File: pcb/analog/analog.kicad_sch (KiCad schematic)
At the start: 72 parts, among them J1 USB_C_Receptacle_USB2.0, SW1 SW_Push, SW2 SW_Push, U1 SRV05-4, U10 RP2040, U11 W25Q128JVS, U2 XC6206P332MR, U3 DRV5056A3xDBZxQ1, U4 DRV5056A3xDBZxQ1, U5 DRV5056A3xDBZxQ1, U6 74AHCT1G125, U7 74AHCT1G125, U8 74AHCT1G125, U9 74AHCT1G125, Y1 12MHz

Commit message: refactor: drive switch LEDs from a single output pin
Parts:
- removed R7, R8: 1k, Resistor_SMD:R_0402_1005Metric, symbol Device:R_Small
- removed U7, U8: 74AHCT1G125, Package_TO_SOT_SMD:SOT-353_SC-70-5, symbol 74xGxx:74AHCT1G125
- renumbered R12 to R10, R13 to R11, R14 to R12, R15 to R13, R16 to R14, R9 to R7, R10 to R8, R11 to R9, U9 to U7, U10 to U8, U11 to U9
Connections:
- net RGB_HS0: no longer U6.2
- net at LED1.2 (DOUT): now also LED2.3 (DIN)
- net at LED3.3 (DIN): now also LED2.2 (DOUT)
- net RGB_HS1: no longer names the net of U8.13 (GPIO10)
- net RGB_HS2: no longer names the net of U8.12 (GPIO9)
- new net RGB_HS: U6.2
- no-connect marks 8 -> 6
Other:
- moved on the sheet: C1, C10, C11, C2, C3, C6, C7, C8, C9, LED1, LED2, LED3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

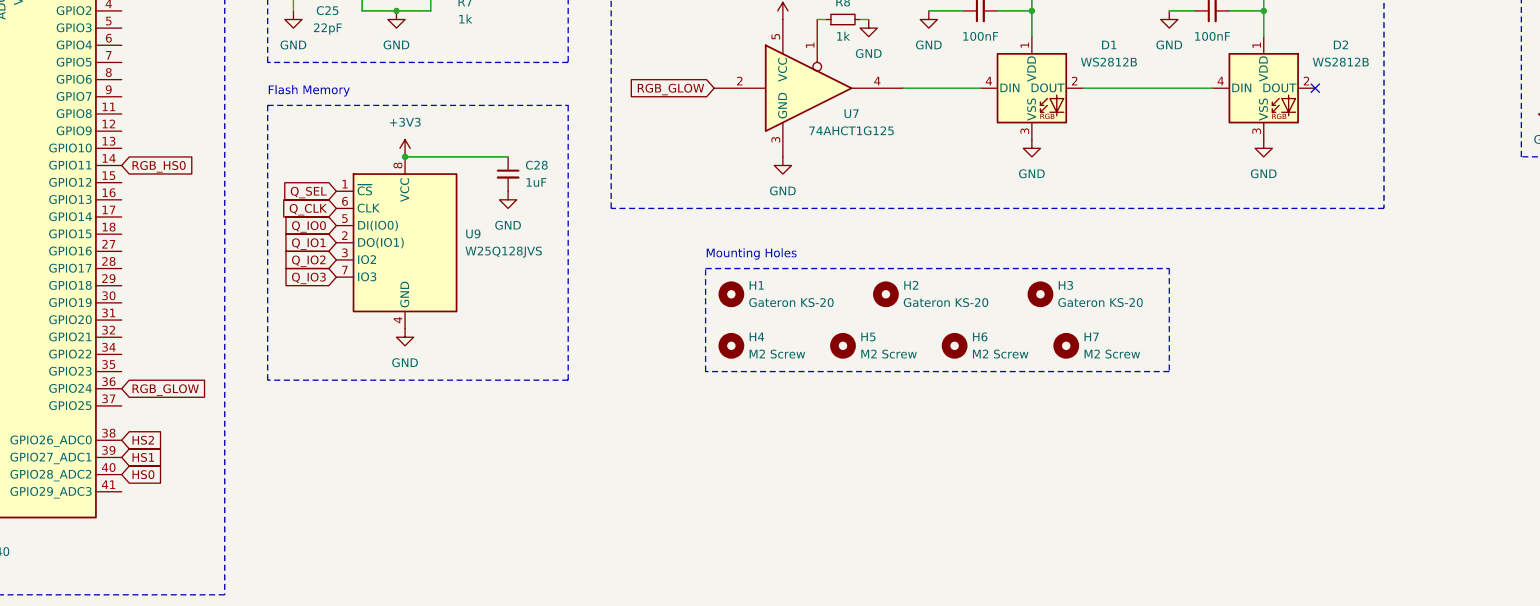
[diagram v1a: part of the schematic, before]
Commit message: feat: routing for new pcb required shuffling some components around, but this casn be accounted for in software, so it's not a big deal.
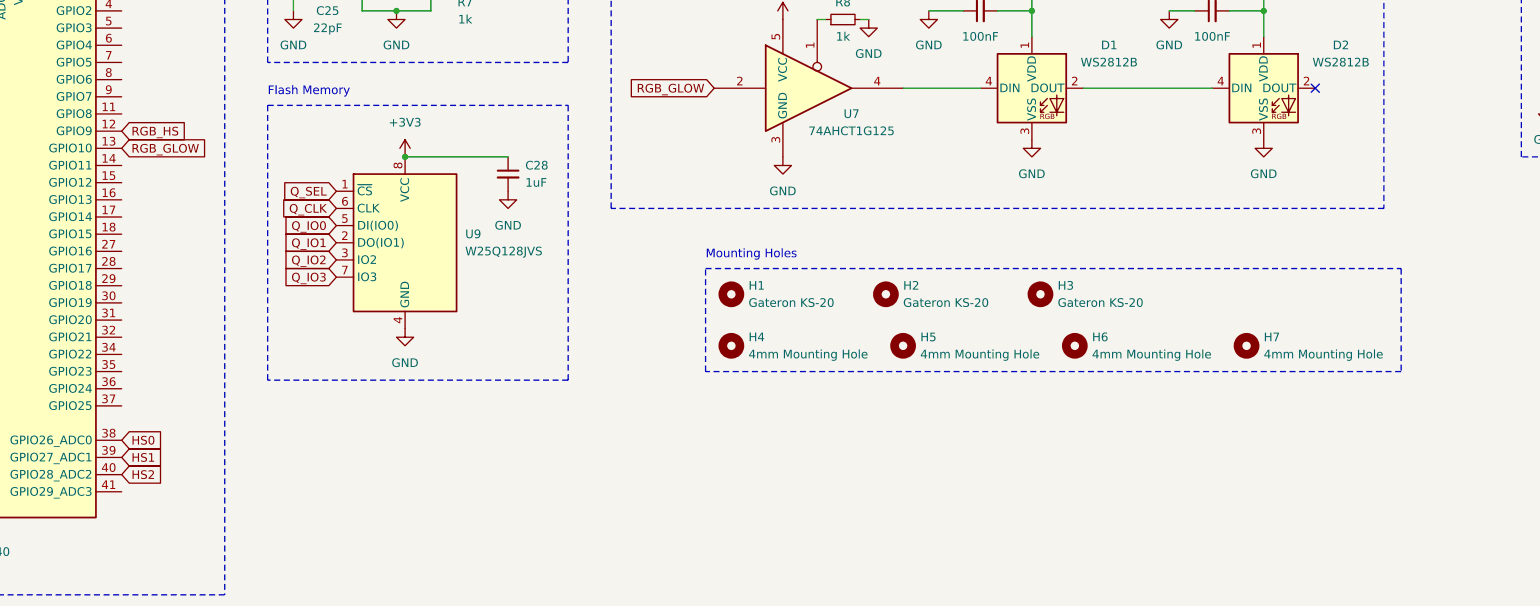
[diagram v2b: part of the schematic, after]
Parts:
- H4, H5, H6, H7: value M2 Screw -> 4mm Mounting Hole; footprint MountingHole:MountingHole_2.2mm_M2 -> MountingHole:MountingHole_4mm
- J1: footprint Connector_USB:USB_C_Receptacle_HRO_TYPE-C-31-M-12 -> PCM_marbastlib-various:USB_C_Receptacle_HRO_TYPE-C-31-M-12
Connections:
- net HS0: now also U8.38 (GPIO26_ADC0); no longer U8.40 (GPIO28_ADC2)
- net HS2: now also U8.40 (GPIO28_ADC2); no longer U8.38 (GPIO26_ADC0)
- net RGB_GLOW: now also U8.13 (GPIO10); no longer U8.36 (GPIO24)
- net RGB_HS: now also U8.12 (GPIO9)
- net RGB_HS0: no longer names the net of U8.14 (GPIO11)
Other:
- moved on the sheet: H5, H6, H7
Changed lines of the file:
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@@
     (fill (type none))
   )
-  (rectangle (start 173.99 168.91) (end 242.57 184.15)
+  (rectangle (start 173.99 168.91) (end 276.86 184.15)
     (stroke (width 0) (type dash))
     (fill (type none))
@@
     )
   )
-  (global_label "RGB_GLOW" (shape input) (at 87.63 186.69 0) (fields_autoplaced)
-    (effects (font (size 1.27 1.27)) (justify left))
-    (property "Intersheetrefs" "${INTERSHEET_REFS}" (at 100.4728 186.69 0)
-      (effects (font (size 1.27 1.27)) (justify left) hide)
-    )
-  )
   (global_label "XIN" (shape input) (at 36.83 171.45 180) (fields_autoplaced)
     (effects (font (size 1.27 1.27)) (justify right))
@@
     )
   )
-  (global_label "HS2" (shape input) (at 87.63 194.31 0) (fields_autoplaced)
+  (global_label "HS2" (shape input) (at 87.63 199.39 0) (fields_autoplaced)
     (effects (font (size 1.27 1.27)) (justify left))
-    (property "Intersheetrefs" "${INTERSHEET_REFS}" (at 94.3647 194.31 0)
+    (property "Intersheetrefs" "${INTERSHEET_REFS}" (at 94.3647 199.39 0)
       (effects (font (size 1.27 1.27)) (justify left) hide)
     )
@@
     )
   )
+  (global_label "RGB_GLOW" (shape input) (at 87.63 151.13 0) (fields_autoplaced)
+    (effects (font (size 1.27 1.27)) (justify left))
+    (property "Intersheetrefs" "${INTERSHEET_REFS}" (at 100.4728 151.13 0)
+      (effects (font (size 1.27 1.27)) (justify left) hide)
+    )
+  )
   (global_label "XOUT" (shape input) (at 143.51 127 0) (fields_autoplaced)
     (effects (font (size 1.27 1.27)) (justify left))
@@
     )
   )
-  (global_label "RGB_HS0" (shape input) (at 87.63 153.67 0) (fields_autoplaced)
+  (global_label "RGB_HS" (shape input) (at 87.63 148.59 0) (fields_autoplaced)
     (effects (font (size 1.27 1.27)) (justify left))
-    (property "Intersheetrefs" "${INTERSHEET_REFS}" (at 99.1423 153.67 0)
+    (property "Intersheetrefs" "${INTERSHEET_REFS}" (at 97.9328 148.59 0)
       (effects (font (size 1.27 1.27)) (justify left) hide)
     )
@@
     )
   )
-  (global_label "HS0" (shape input) (at 87.63 199.39 0) (fields_autoplaced)
+  (global_label "HS0" (shape input) (at 87.63 194.31 0) (fields_autoplaced)
     (effects (font (size 1.27 1.27)) (justify left))
-    (property "Intersheetrefs" "${INTERSHEET_REFS}" (at 94.3647 199.39 0)
+    (property "Intersheetrefs" "${INTERSHEET_REFS}" (at 94.3647 194.31 0)
       (effects (font (size 1.27 1.27)) (justify left) hide)
     )
@@
     )
   )
-  (symbol (lib_id "Mechanical:MountingHole") (at 194.31 180.34 0) (unit 1)
+  (symbol (lib_id "Mechanical:MountingHole") (at 203.2 180.34 0) (unit 1)
     (in_bom yes) (on_board yes) (dnp no) (fields_autoplaced)
-    (property "Reference" "H5" (at 196.85 179.07 0)
+    (property "Reference" "H5" (at 205.74 179.07 0)
       (effects (font (size 1.27 1.27)) (justify left))
     )
-    (property "Value" "M2 Screw" (at 196.85 181.61 0)
+    (property "Value" "4mm Mounting Hole" (at 205.74 181.61 0)
       (effects (font (size 1.27 1.27)) (justify left))
     )
-    (property "Footprint" "MountingHole:MountingHole_2.2mm_M2" (at 194.31 180.34 0)
+    (property "Footprint" "MountingHole:MountingHole_4mm" (at 203.2 180.34 0)
       (effects (font (size 1.27 1.27)) hide)
     )
-    (property "Datasheet" "~" (at 194.31 180.34 0)
+    (property "Datasheet" "~" (at 203.2 180.34 0)
       (effects (font (size 1.27 1.27)) hide)
     )
@@
     )
   )
-  (symbol (lib_id "Mechanical:MountingHole") (at 210.82 180.34 0) (unit 1)
+  (symbol (lib_id "Mechanical:MountingHole") (at 228.6 180.34 0) (unit 1)
     (in_bom yes) (on_board yes) (dnp no) (fields_autoplaced)
-    (property "Reference" "H6" (at 213.36 179.07 0)
+    (property "Reference" "H6" (at 231.14 179.07 0)
       (effects (font (size 1.27 1.27)) (justify left))
     )
-    (property "Value" "M2 Screw" (at 213.36 181.61 0)
+    (property "Value" "4mm Mounting Hole" (at 231.14 181.61 0)
       (effects (font (size 1.27 1.27)) (justify left))
     )
-    (property "Footprint" "MountingHole:MountingHole_2.2mm_M2" (at 210.82 180.34 0)
+    (property "Footprint" "MountingHole:MountingHole_4mm" (at 228.6 180.34 0)
       (effects (font (size 1.27 1.27)) hide)
     )
-    (property "Datasheet" "~" (at 210.82 180.34 0)
+    (property "Datasheet" "~" (at 228.6 180.34 0)
       (effects (font (size 1.27 1.27)) hide)
     )
@@
       (effects (font (size 1.27 1.27)))
     )
-    (property "Footprint" "Connector_USB:USB_C_Receptacle_HRO_TYPE-C-31-M-12" (at 33.02 43.18 0)
+    (property "Footprint" "PCM_marbastlib-various:USB_C_Receptacle_HRO_TYPE-C-31-M-12" (at 33.02 43.18 0)
       (effects (font (size 1.27 1.27)) hide)
     )
@@
       (effects (font (size 1.27 1.27)) (justify left))
     )
-    (property "Value" "M2 Screw" (at 180.34 181.61 0)
+    (property "Value" "4mm Mounting Hole" (at 180.34 181.61 0)
       (effects (font (size 1.27 1.27)) (justify left))
     )
-    (property "Footprint" "MountingHole:MountingHole_2.2mm_M2" (at 177.8 180.34 0)
+    (property "Footprint" "MountingHole:MountingHole_4mm" (at 177.8 180.34 0)
       (effects (font (size 1.27 1.27)) hide)
     )
@@
     )
   )
-  (symbol (lib_id "Mechanical:MountingHole") (at 227.33 180.34 0) (unit 1)
+  (symbol (lib_id "Mechanical:MountingHole") (at 254 180.34 0) (unit 1)
     (in_bom yes) (on_board yes) (dnp no) (fields_autoplaced)
-    (property "Reference" "H7" (at 229.87 179.07 0)
+    (property "Reference" "H7" (at 256.54 179.07 0)
       (effects (font (size 1.27 1.27)) (justify left))
     )
-    (property "Value" "M2 Screw" (at 229.87 181.61 0)
+    (property "Value" "4mm Mounting Hole" (at 256.54 181.61 0)
       (effects (font (size 1.27 1.27)) (justify left))
     )
-    (property "Footprint" "MountingHole:MountingHole_2.2mm_M2" (at 227.33 180.34 0)
+    (property "Footprint" "MountingHole:MountingHole_4mm" (at 254 180.34 0)
       (effects (font (size 1.27 1.27)) hide)
     )
-    (property "Datasheet" "~" (at 227.33 180.34 0)
+    (property "Datasheet" "~" (at 254 180.34 0)
       (effects (font (size 1.27 1.27)) hide)
     )

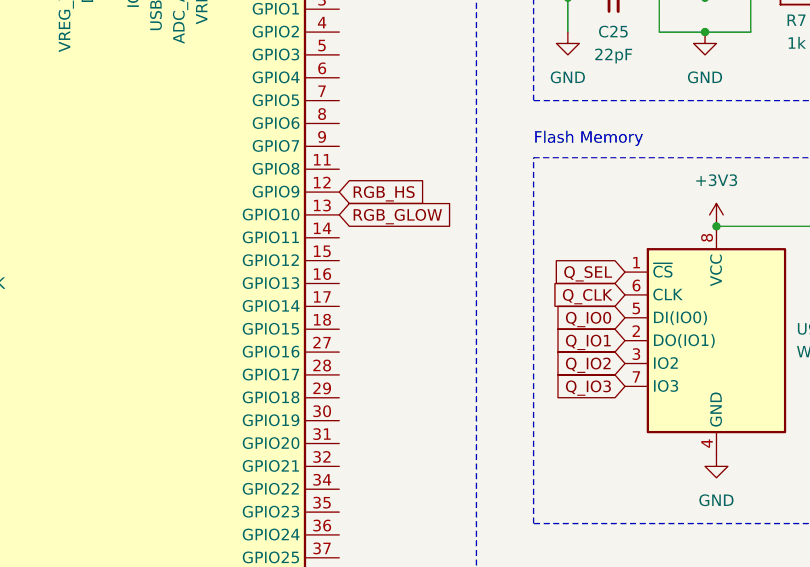
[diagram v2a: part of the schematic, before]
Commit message: refactor: new pcb layout
more compact and has fewer crossing lines. can definitely shrink the PCB, but I've picked this size so it's possible to see the design from the top.
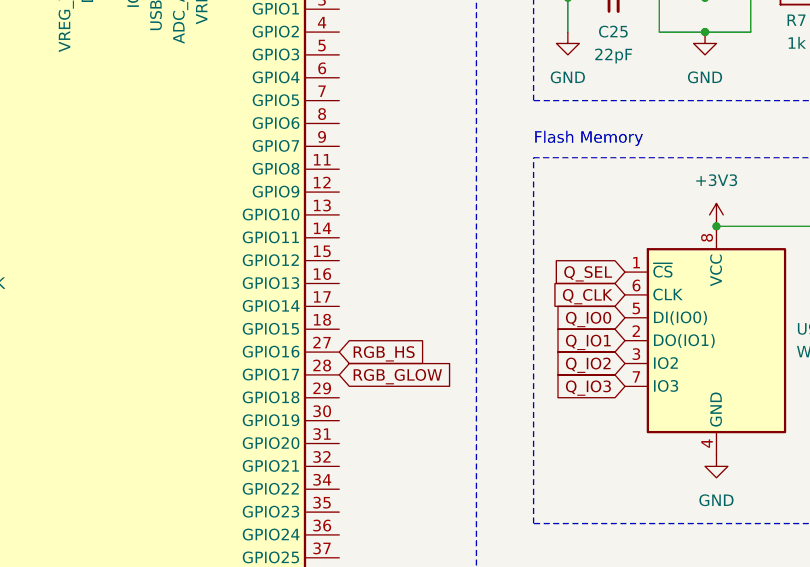
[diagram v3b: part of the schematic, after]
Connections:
- net RGB_GLOW: now also U8.28 (GPIO17); no longer U8.13 (GPIO10)
- net RGB_HS: now also U8.27 (GPIO16); no longer U8.12 (GPIO9)
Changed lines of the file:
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@@
     )
   )
-  (global_label "RGB_GLOW" (shape input) (at 87.63 151.13 0) (fields_autoplaced)
+  (global_label "RGB_GLOW" (shape input) (at 87.63 168.91 0) (fields_autoplaced)
     (effects (font (size 1.27 1.27)) (justify left))
-    (property "Intersheetrefs" "${INTERSHEET_REFS}" (at 100.4728 151.13 0)
+    (property "Intersheetrefs" "${INTERSHEET_REFS}" (at 100.4728 168.91 0)
       (effects (font (size 1.27 1.27)) (justify left) hide)
     )
@@
     )
   )
-  (global_label "RGB_HS" (shape input) (at 87.63 148.59 0) (fields_autoplaced)
+  (global_label "RGB_HS" (shape input) (at 87.63 166.37 0) (fields_autoplaced)
     (effects (font (size 1.27 1.27)) (justify left))
-    (property "Intersheetrefs" "${INTERSHEET_REFS}" (at 97.9328 148.59 0)
+    (property "Intersheetrefs" "${INTERSHEET_REFS}" (at 97.9328 166.37 0)
       (effects (font (size 1.27 1.27)) (justify left) hide)
     )

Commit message: refactor: create custom footprint for KS-20 w/ DRV5056
this includes a custom silkscreen, reference value and a rule area to disallow copper fills in the middle of the sensor.
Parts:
- removed H1, H2, H3: Gateron KS-20, Custom:MX-1U-NoPins, symbol Mechanical:MountingHole
- U3, U4, U5: footprint Package_TO_SOT_SMD:SOT-23 -> Custom:KS-20-1U-DRV5056
- renumbered H4 to H1, H5 to H2, H6 to H3, H7 to H4
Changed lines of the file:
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@@
     )
   )
-  (symbol (lib_id "Mechanical:MountingHole") (at 200.66 172.72 0) (unit 1)
-    (in_bom yes) (on_board yes) (dnp no) (fields_autoplaced)
-    (property "Reference" "H2" (at 203.2 171.45 0)
-      (effects (font (size 1.27 1.27)) (justify left))
-    )
-    (property "Value" "Gateron KS-20" (at 203.2 173.99 0)
-      (effects (font (size 1.27 1.27)) (justify left))
-    )
-    (property "Footprint" "Custom:MX-1U-NoPins" (at 200.66 172.72 0)
-      (effects (font (size 1.27 1.27)) hide)
-    )
-    (property "Datasheet" "~" (at 200.66 172.72 0)
-      (effects (font (size 1.27 1.27)) hide)
-    )
-    (instances
-      (project "analog"
-        (path "/a63f8075-a969-4b1c-b924-6f5af0e1e9e2"
-          (reference "H2") (unit 1)
-        )
-      )
-      (project "pcb"
-        (path "/fe0c1c23-b294-4653-a8db-85682224ef67"
-          (reference "H2") (unit 1)
-        )
-      )
-    )
-  )
   (symbol (lib_id "LED:WS2812B") (at 222.25 142.24 0) (unit 1)
     (in_bom yes) (on_board yes) (dnp no)
@@
       (effects (font (size 1.27 1.27)) (justify right))
     )
-    (property "Footprint" "Package_TO_SOT_SMD:SOT-23" (at 186.69 44.45 0)
+    (property "Footprint" "Custom:KS-20-1U-DRV5056" (at 186.69 44.45 0)
       (effects (font (size 1.27 1.27)) hide)
     )
@@
     )
   )
-  (symbol (lib_id "Mechanical:MountingHole") (at 177.8 172.72 0) (unit 1)
-    (in_bom yes) (on_board yes) (dnp no) (fields_autoplaced)
-    (property "Reference" "H1" (at 180.34 171.45 0)
-      (effects (font (size 1.27 1.27)) (justify left))
-    )
-    (property "Value" "Gateron KS-20" (at 180.34 173.99 0)
-      (effects (font (size 1.27 1.27)) (justify left))
-    )
-    (property "Footprint" "Custom:MX-1U-NoPins" (at 177.8 172.72 0)
-      (effects (font (size 1.27 1.27)) hide)
-    )
-    (property "Datasheet" "~" (at 177.8 172.72 0)
-      (effects (font (size 1.27 1.27)) hide)
-    )
-    (instances
-      (project "analog"
-        (path "/a63f8075-a969-4b1c-b924-6f5af0e1e9e2"
-          (reference "H1") (unit 1)
-        )
-      )
-      (project "pcb"
-        (path "/fe0c1c23-b294-4653-a8db-85682224ef67"
-          (reference "H1") (unit 1)
-        )
-      )
-    )
-  )
   (symbol (lib_id "Device:C_Small") (at 86.36 91.44 0) (unit 1)
     (in_bom yes) (on_board yes) (dnp no) (fields_autoplaced)
@@
   (symbol (lib_id "Mechanical:MountingHole") (at 203.2 180.34 0) (unit 1)
     (in_bom yes) (on_board yes) (dnp no) (fields_autoplaced)
-    (property "Reference" "H5" (at 205.74 179.07 0)
+    (property "Reference" "H2" (at 205.74 179.07 0)
       (effects (font (size 1.27 1.27)) (justify left))
     )
@@
       (project "analog"
         (path "/a63f8075-a969-4b1c-b924-6f5af0e1e9e2"
-          (reference "H5") (unit 1)
+          (reference "H2") (unit 1)
         )
       )
@@
       (effects (font (size 1.27 1.27)) (justify right))
     )
-    (property "Footprint" "Package_TO_SOT_SMD:SOT-23" (at 303.53 44.45 0)
+    (property "Footprint" "Custom:KS-20-1U-DRV5056" (at 303.53 44.45 0)
       (effects (font (size 1.27 1.27)) hide)
     )
@@
   (symbol (lib_id "Mechanical:MountingHole") (at 228.6 180.34 0) (unit 1)
     (in_bom yes) (on_board yes) (dnp no) (fields_autoplaced)
-    (property "Reference" "H6" (at 231.14 179.07 0)
+    (property "Reference" "H3" (at 231.14 179.07 0)
       (effects (font (size 1.27 1.27)) (justify left))
     )
@@
       (project "analog"
         (path "/a63f8075-a969-4b1c-b924-6f5af0e1e9e2"
-          (reference "H6") (unit 1)
+          (reference "H3") (unit 1)
         )
       )
@@
       (effects (font (size 1.27 1.27)) (justify right))
     )
-    (property "Footprint" "Package_TO_SOT_SMD:SOT-23" (at 245.11 44.45 0)
+    (property "Footprint" "Custom:KS-20-1U-DRV5056" (at 245.11 44.45 0)
       (effects (font (size 1.27 1.27)) hide)
     )
@@
     )
   )
-  (symbol (lib_id "Mechanical:MountingHole") (at 223.52 172.72 0) (unit 1)
-    (in_bom yes) (on_board yes) (dnp no) (fields_autoplaced)
-    (property "Reference" "H3" (at 226.06 171.45 0)
-      (effects (font (size 1.27 1.27)) (justify left))
-    )
-    (property "Value" "Gateron KS-20" (at 226.06 173.99 0)
-      (effects (font (size 1.27 1.27)) (justify left))
-    )
-    (property "Footprint" "Custom:MX-1U-NoPins" (at 223.52 172.72 0)
-      (effects (font (size 1.27 1.27)) hide)
-    )
-    (property "Datasheet" "~" (at 223.52 172.72 0)
-      (effects (font (size 1.27 1.27)) hide)
-    )
-    (instances
-      (project "analog"
-        (path "/a63f8075-a969-4b1c-b924-6f5af0e1e9e2"
-          (reference "H3") (unit 1)
-        )
-      )
-      (project "pcb"
-        (path "/fe0c1c23-b294-4653-a8db-85682224ef67"
-          (reference "H3") (unit 1)
-        )
-      )
-    )
-  )
   (symbol (lib_id "Device:R_Small") (at 259.08 44.45 90) (unit 1)
     (in_bom yes) (on_board yes) (dnp no)
@@
   )
   (symbol (lib_id "Mechanical:MountingHole") (at 177.8 180.34 0) (unit 1)
-    (in_bom yes) (on_board yes) (dnp no) (fields_autoplaced)
-    (property "Reference" "H4" (at 180.34 179.07 0)
+    (in_bom yes) (on_board yes) (dnp no)
+    (property "Reference" "H1" (at 180.34 179.07 0)
       (effects (font (size 1.27 1.27)) (justify left))
     )
@@
       (project "analog"
         (path "/a63f8075-a969-4b1c-b924-6f5af0e1e9e2"
-          (reference "H4") (unit 1)
+          (reference "H1") (unit 1)
         )
       )
@@
   (symbol (lib_id "Mechanical:MountingHole") (at 254 180.34 0) (unit 1)
     (in_bom yes) (on_board yes) (dnp no) (fields_autoplaced)
-    (property "Reference" "H7" (at 256.54 179.07 0)
+    (property "Reference" "H4" (at 256.54 179.07 0)
       (effects (font (size 1.27 1.27)) (justify left))
     )
@@
       (project "analog"
         (path "/a63f8075-a969-4b1c-b924-6f5af0e1e9e2"
-          (reference "H7") (unit 1)
+          (reference "H4") (unit 1)
         )
       )
